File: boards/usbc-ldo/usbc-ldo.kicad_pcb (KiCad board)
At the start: 2 copper layers, 40 x 24 mm, 12 parts, among them J1 USB-C, U1 AMS1117-3.3

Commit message: usbc-ldo: LP38693MP-3.3 + 4.7uF caps (USB inrush and low-VBUS dropout fixed)
AMS1117 dropped out of regulation at USB's 4.4V minimum and C2 10uF + C3 22uF
injected 124 uC on hot-plug (USB 2.0 limit 50 uC). AP2112K fixed both but its
6.5V absolute max is below the simulated 6.77V hot-plug overshoot.
LP38693 (12V abs max, 0.33V dropout) passes all three; sim compares v1/v2/v3.
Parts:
- C2: value 10uF -> 4.7uF
- C3: value 22uF -> 4.7uF
- U1: value AMS1117-3.3 -> LP38693MP-3.3; footprint Package_TO_SOT_SMD:SOT-223-3_TabPin2 -> Package_TO_SOT_SMD:SOT-223-5
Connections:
- U1 pad 1: GND -> +5V
- U1 pad 2: +3V3 -> unconnected-(U1-NC-Pad2)
- U1 pad 3: +5V -> +3V3
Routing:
- net Net-(D1-A): track 36.9 -> 22.4 mm, vias 2 -> 3
- net +5V: track 32.3 -> 41.6 mm, vias 0 -> 2
- net GND: track 102.1 -> 94.0 mm, vias 2 -> 0
- net +3V3: track 16.5 -> 15.9 mm, vias 0 -> 2
- net Net-(J1-CC1): track 7.35 -> 7.86 mm

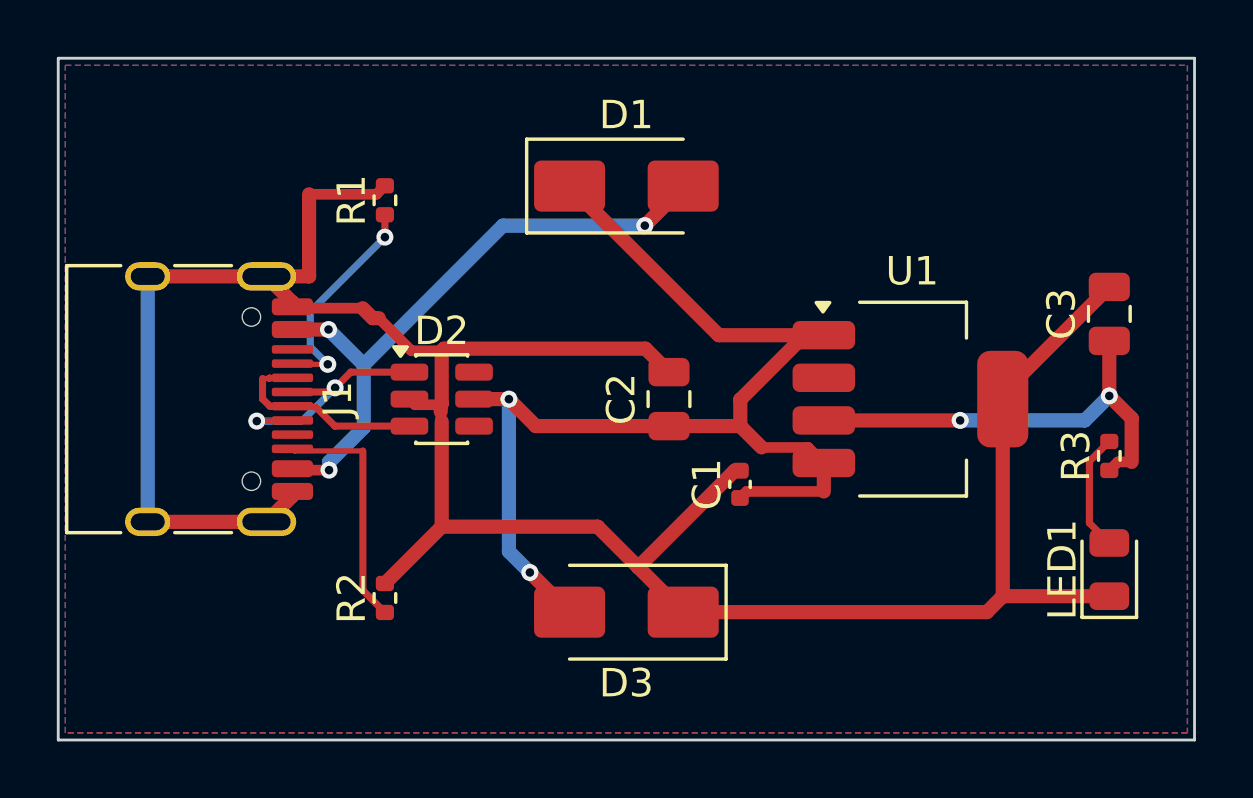
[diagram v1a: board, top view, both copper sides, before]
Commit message: fab: Gerber/drill zip + JLCPCB BOM/CPL with self-checks; USBLC6-2SC6 to match SOT-23-6
lib/fab.py runs as the last build step on all three boards. It refuses to
write the zip when a required Gerber layer is missing or empty, when the
drill-hit count differs from vias + plated/NPTH pad holes (route-format
slots counted once), or when BOM / CPL / board refdes sets disagree.

It also compares each symbol's library default footprint with the one
actually assigned. That caught all three boards using the USBLC6-2P6
symbol (SOT-666) on a SOT-23-6 footprint: electrically identical pinout,
so ERC/DRC/netlist checks passed, but a BOM ordered by value would buy a
part that does not fit. Switched to USBLC6-2SC6.

LCSC part numbers come from a hand-checked boards/<b>/lcsc.json; the
script never guesses them and lists missing rows in fab/missing-lcsc.txt.
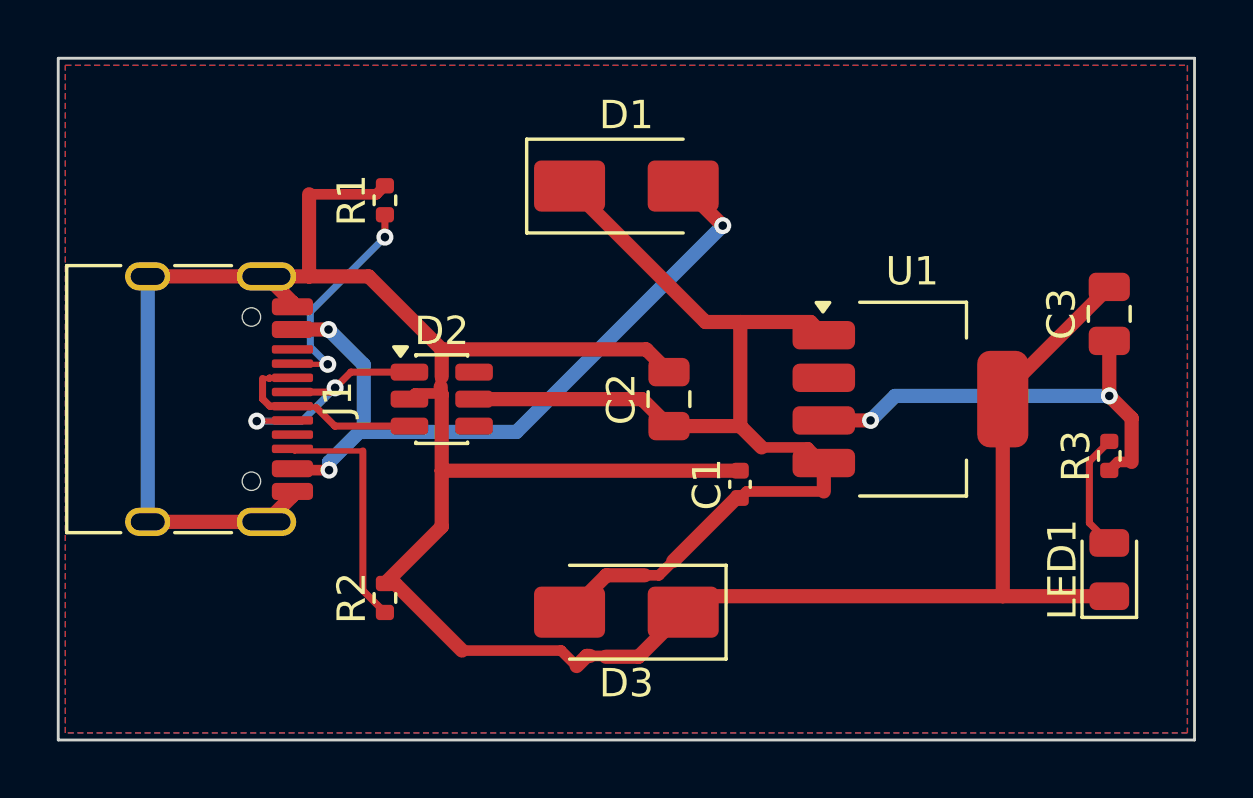
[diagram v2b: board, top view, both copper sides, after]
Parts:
- D2: value USBLC6-2P6 -> USBLC6-2SC6
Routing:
- net GND: track 94.0 -> 102.1 mm
- net Net-(D1-A): track 22.4 -> 26.3 mm
- net +5V: track 41.6 -> 39.7 mm, vias 2 -> 0

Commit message: fab: verified LCSC part numbers for all three boards; BOM/CPL ready to upload
lib/lcsc.py checks every hand-written part number in boards/<b>/lcsc.json
against the JLCPCB parts API: the part exists, its model equals the one
written down, stock covers 5 boards, the package matches what the KiCad
footprint name implies (0402/0805, SOT-23(-6), SOT-223-5, SMA, SOIC-W,
CP_Elec, 2.54 mm headers), resistor/capacitor values match the JLC
attributes and LED colours match. A mutation test (1k part for a 10k
resistor, wrong model, 0805 part on a 0402 footprint, missing row) fails
all four. Results go to lcsc-check.json with a hash of lcsc.json, so the
build itself stays offline and refuses a stale check.

fab.py now writes BOM/CPL only for assembled parts, lists parts LCSC
cannot supply in hand-solder.csv (relay8: mains terminals and fuse
holders), applies lib/jlc_rotations.json to the CPL and writes
rotation-review.csv. None of the rotation corrections are verified on
hardware; every row says so.
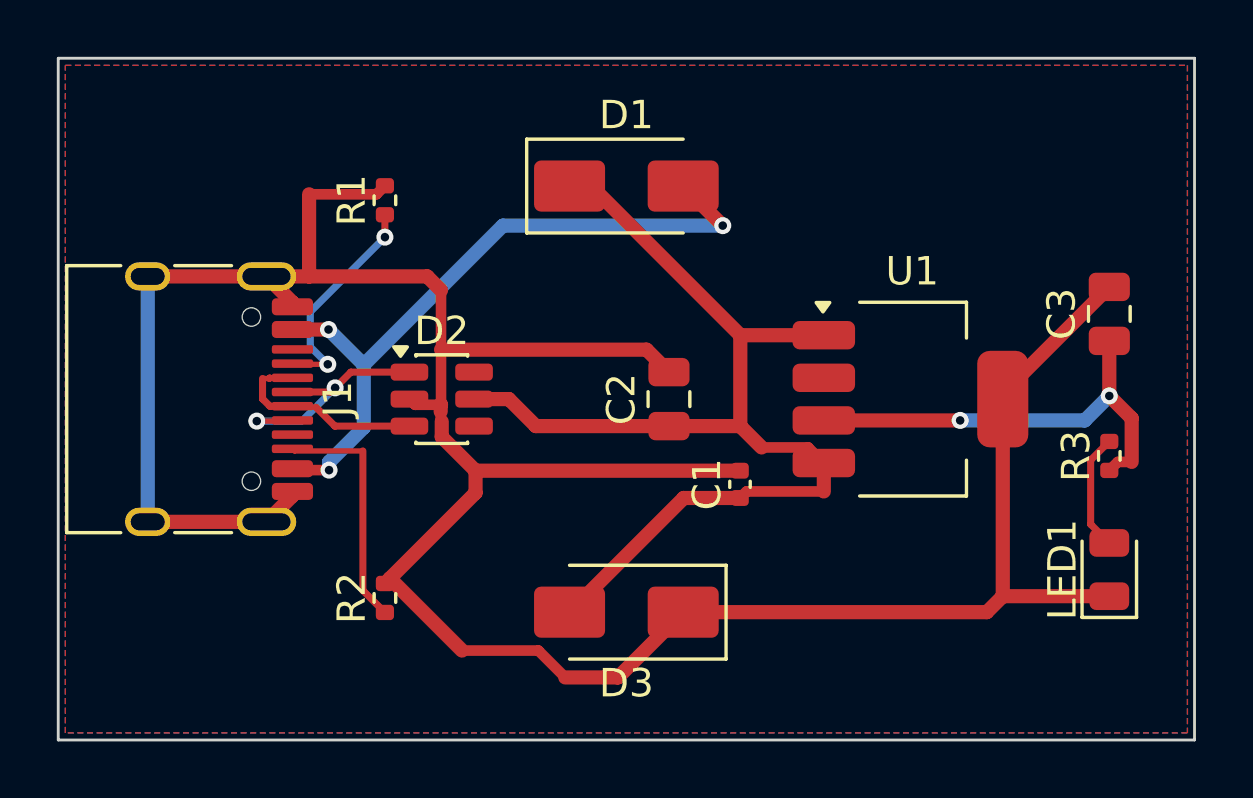
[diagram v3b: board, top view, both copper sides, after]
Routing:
- net GND: track 102.1 -> 103.3 mm
- net Net-(D1-A): track 26.3 -> 25.2 mm

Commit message: review: datasheet design review on the netlist; fixes a reversed TVS and dim LEDs
lib/review.py checks the design intent that ERC and the netlist check take
on trust: diode/TVS polarity against inferred rail voltages, LED current
from the JLC Vf range, per-datasheet decoupling and supply ranges, USB-C
CC pull-downs and D+/D- on both sides, ESP32-C3 EN RC, strapping pins and
GPIO18/19, relay flyback path and pickup voltage, capacitor rating and
polarity. It runs after the netlist check and stops the build on ERROR.
lib/review_test.py breaks the real netlists 15 ways; every rule fires and
the unmodified boards report no ERROR.

Real defects it found:
- usbc-ldo: SMAJ5.0A had anode on +5V and cathode on GND (KiCad names
  the cathode pin "A1"), shorting the rail on plug-in. Swapped.
- esp32c3: blue user LED on a 3.3 V GPIO (Vf 2.5-3.6 V) -> yellow, 470R.
- esp32c3, relay8: green power LED at ~0.45 mA through 1k -> 220R.
- usbc-ldo: SS32 symbol for an SS34 part -> Diode:SS34.

Also: lcsc-check.json keeps JLC attributes (Vf, voltage rating) for the
review; lcsc.py groups parts from net.txt instead of fab/groups.json; the
build retries freerouting (up to 3 runs) because it is not deterministic
and occasionally leaves two connections unrouted on the same DSN.
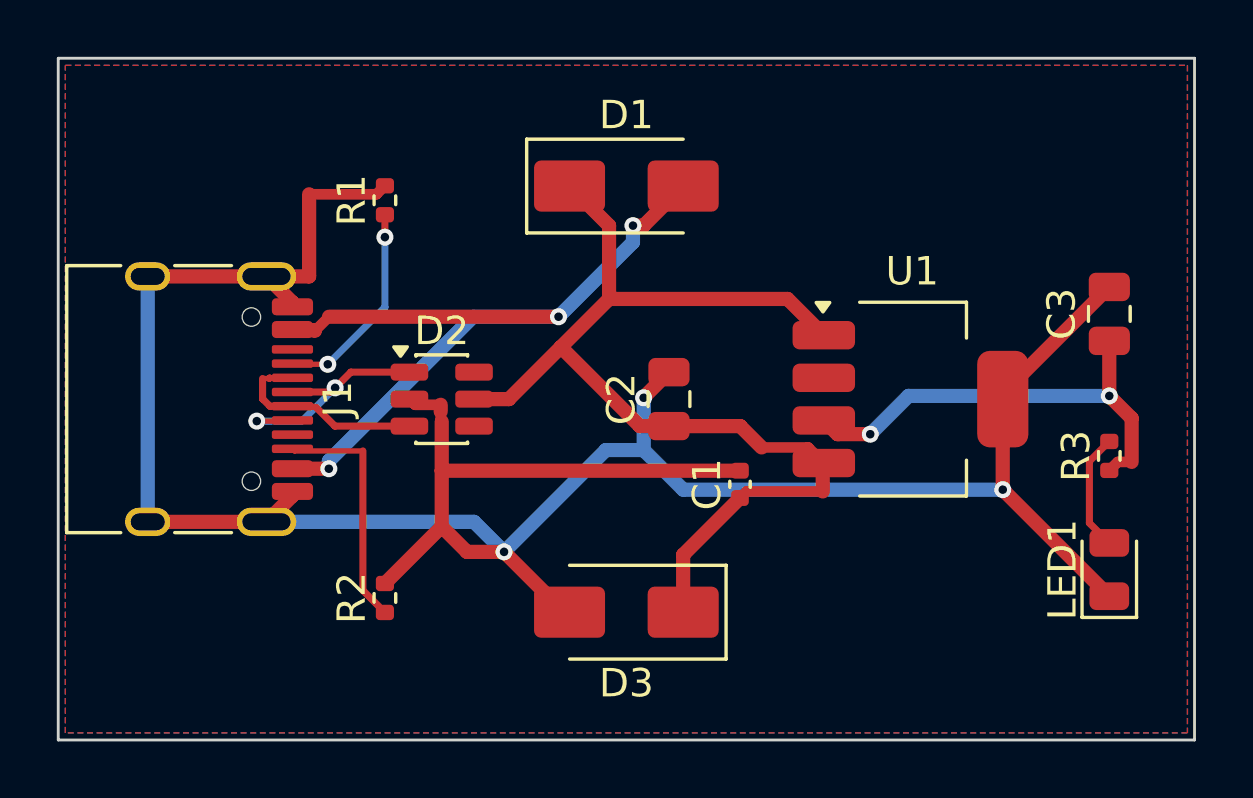
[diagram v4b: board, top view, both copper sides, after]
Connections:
- D3 pad 1: GND -> +5V
- D3 pad 2: +5V -> GND
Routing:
- net GND: track 103.3 -> 97.2 mm, vias 0 -> 3
- net Net-(D1-A): track 25.2 -> 28.0 mm
- net +5V: track 39.3 -> 38.7 mm
- net Net-(J1-CC1): track 7.86 -> 7.35 mm

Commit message: build: reproducible output (seeded UUIDs, single-thread freerouting, no retry)
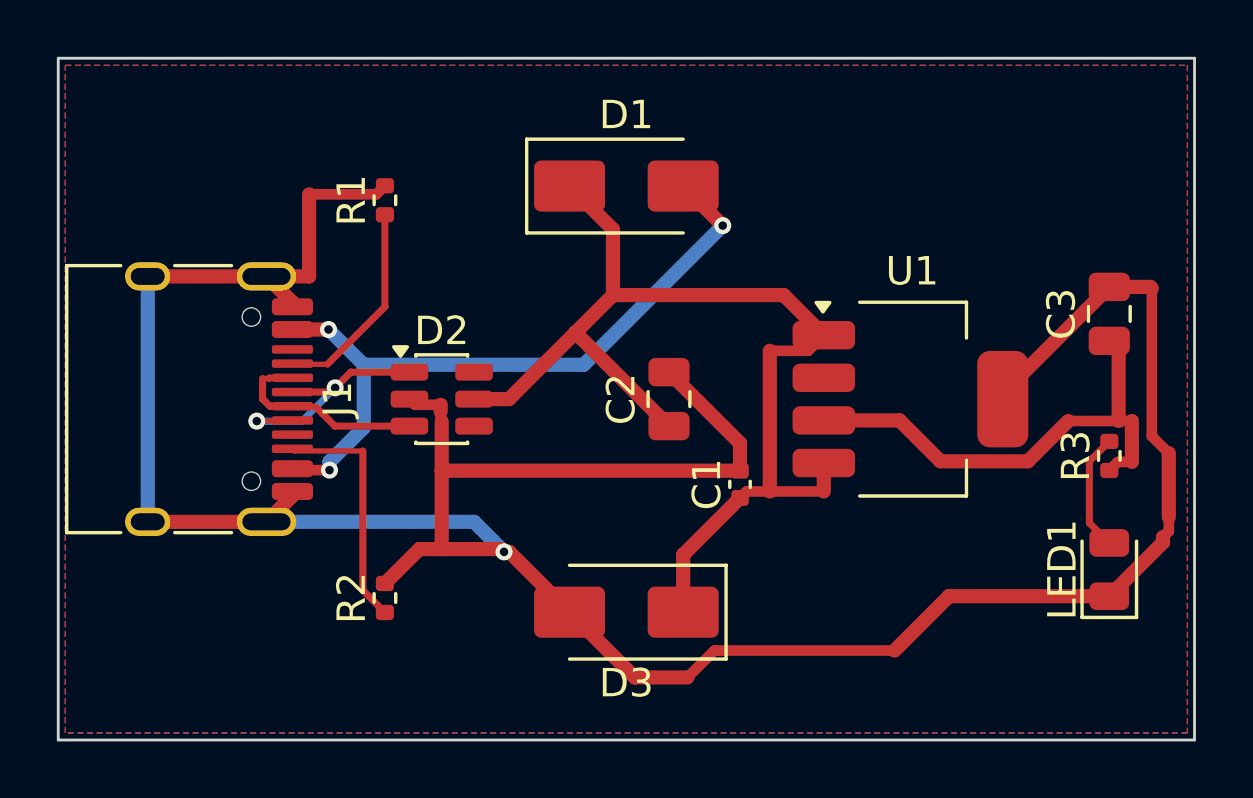
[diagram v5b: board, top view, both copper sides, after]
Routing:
- net GND: track 97.2 -> 105.2 mm, vias 3 -> 1
- net Net-(D1-A): track 28.0 -> 25.2 mm
- net +3V3: track 16.3 -> 17.3 mm, vias 2 -> 0
- net +5V: track 38.7 -> 39.5 mm
- net Net-(J1-CC1): track 7.35 -> 7.34 mm, vias 2 -> 0

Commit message: pcbgen: board-only mounting holes; usbc-ldo gets four M2.5 holes
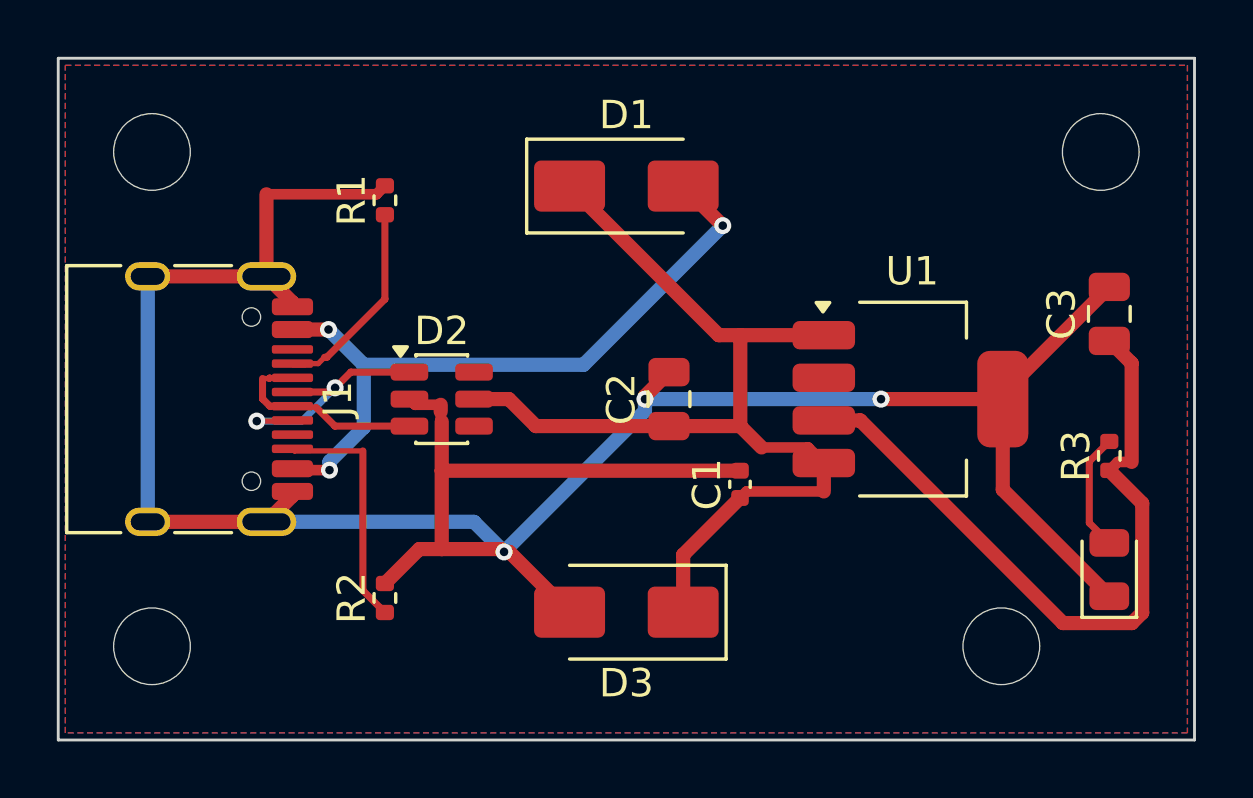
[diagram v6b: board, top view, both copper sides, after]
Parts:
- added H1: MountingHole_2.7mm_M2.5, MountingHole:MountingHole_2.7mm_M2.5, F.Cu at (103.3, 103.3)
- added H2: MountingHole_2.7mm_M2.5, MountingHole:MountingHole_2.7mm_M2.5, F.Cu at (136.7, 103.3)
- added H3: MountingHole_2.7mm_M2.5, MountingHole:MountingHole_2.7mm_M2.5, F.Cu at (103.3, 120.7)
- added H4: MountingHole_2.7mm_M2.5, MountingHole:MountingHole_2.7mm_M2.5, F.Cu at (133.2, 120.7)
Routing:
- net GND: track 105.2 -> 95.9 mm, vias 1 -> 3
- net +3V3: track 17.3 -> 25.3 mm
- net +5V: track 39.5 -> 36.5 mm

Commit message: pcbgen: UUIDs derived from the design so routing is the same on every KiCad 10.0.x (#11)
KIID.SeedGenerator alone is not enough: KiCad 10.0.6 and 10.0.7 consume a
different number of UUIDs while loading footprints, the Specctra exporter
orders by UUID, and freerouting gave 6 vias locally vs 9 on CI.
stable_uuids() sets every item to uuid5(board/ref/kind/index) before each
save that feeds routing. esp32c3: C4 moved 0.66 mm and turned 270 deg; EN
did not route in the new order.
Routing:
- net +5V: track 36.5 -> 38.1 mm, vias 0 -> 2
- net GND: track 95.9 -> 94.5 mm, vias 3 -> 0
- net +3V3: track 25.3 -> 23.9 mm
- net Net-(J1-CC1): track 7.17 -> 7.92 mm, vias 0 -> 2
